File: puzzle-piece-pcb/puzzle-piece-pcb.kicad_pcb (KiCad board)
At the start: 2 copper layers, 27 x 27 mm, 7 parts, among them J1 OLED, J2 Input, J3 PROG_DEBUG, U1 ATtiny1624-SS

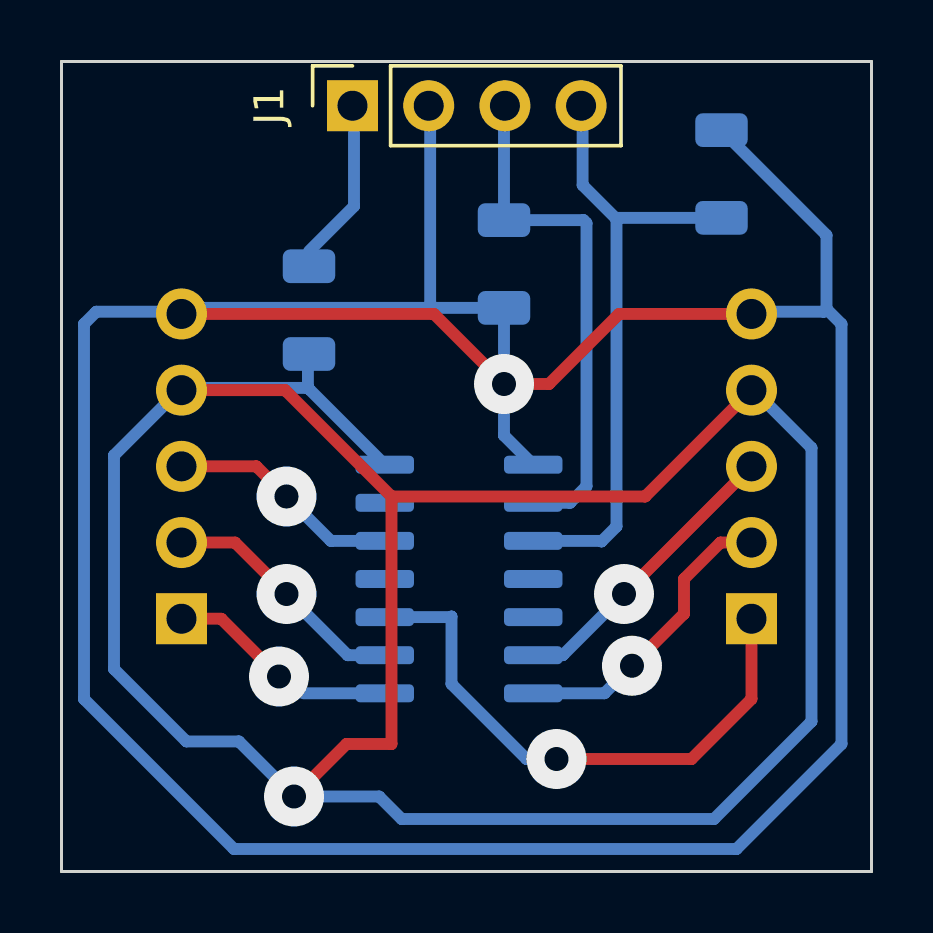
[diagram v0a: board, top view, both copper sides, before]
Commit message: made puzzle piece pcb one sided
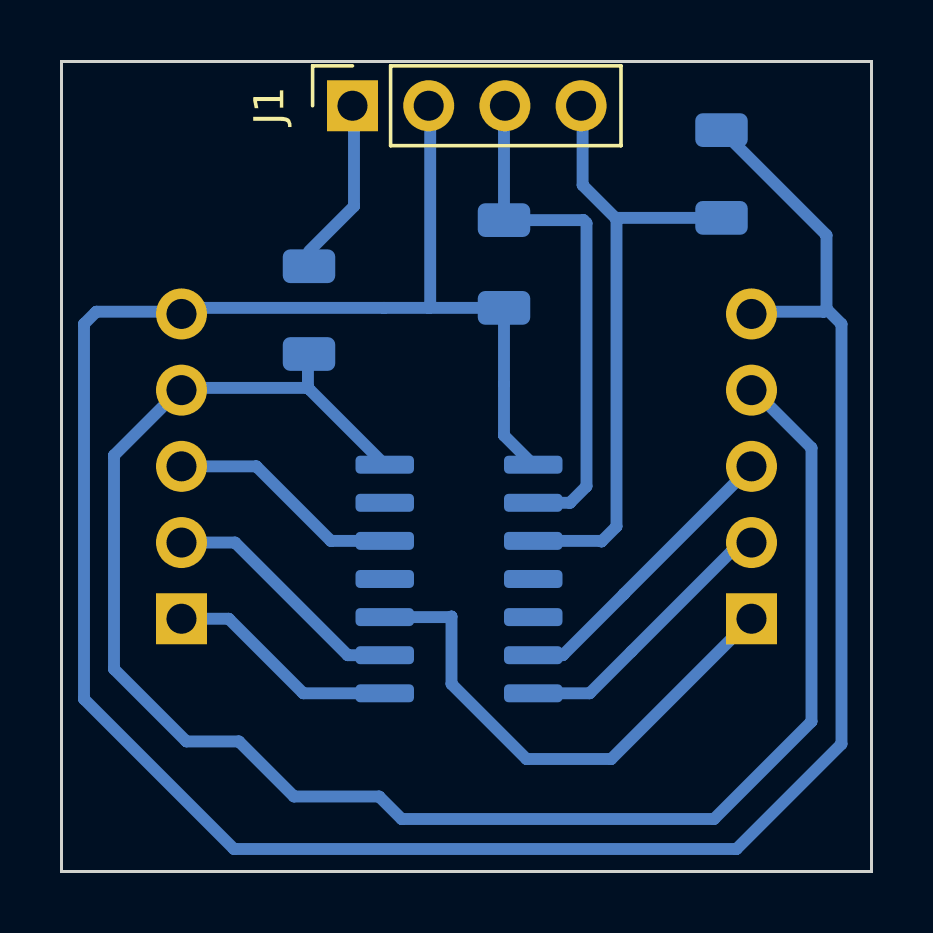
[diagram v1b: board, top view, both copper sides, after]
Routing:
- net OLED_GND : track 97.5 -> 63.3 mm, vias 1 -> 0
- net +3.3V: track 113.4 -> 92.5 mm, vias 1 -> 0
- net UPDI: track 19.0 -> 17.5 mm, vias 1 -> 0
- net H_SDA: track 6.76 -> 7.80 mm, vias 1 -> 0
- net TX: track 10.0 -> 9.36 mm, vias 1 -> 0
- net H_SCL: vias 1 -> 0
- net RX: vias 1 -> 0
- net ANALOG: vias 1 -> 0
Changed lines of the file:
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@@
-	)
-	(segment
-		(start 165 100)
-		(end 166.5 100)
-		(width 0.396748)
-		(layer "F.Cu")
-		(net 3)
-	)
-	(segment
-		(start 154.25 97.665)
-		(end 162.665 97.665)
-		(width 0.396748)
-		(layer "F.Cu")
-		(net 3)
-	)
-	(segment
-		(start 166.5 100)
-		(end 168.835 97.665)
-		(width 0.396748)
-		(layer "F.Cu")
-		(net 3)
-	)
-	(segment
-		(start 168.835 97.665)
-		(end 173.25 97.665)
-		(width 0.396748)
-		(layer "F.Cu")
-		(net 3)
-	)
-	(segment
-		(start 162.665 97.665)
-		(end 165 100)
-		(width 0.396748)
-		(layer "F.Cu")
-		(net 3)
-	)
-	(via
-		(at 165 100)
-		(size 2)
-		(drill 0.8)
-		(layers "F.Cu" "B.Cu")
-		(net 3)
 	)
 	(segment
@@
 	)
 	(segment
-		(start 154.25 102.745)
-		(end 156.745 102.745)
-		(width 0.396748)
-		(layer "F.Cu")
-		(net 4)
-	)
-	(segment
-		(start 156.745 102.745)
-		(end 157.75 103.75)
-		(width 0.396748)
-		(layer "F.Cu")
-		(net 4)
-	)
-	(via
-		(at 157.75 103.75)
-		(size 2)
-		(drill 0.8)
-		(layers "F.Cu" "B.Cu")
-		(net 4)
-	)
-	(segment
 		(start 161.025 105.23)
 		(end 159.23 105.23)
@@
 	(segment
 		(start 159.23 105.23)
-		(end 157.75 103.75)
+		(end 156.745 102.745)
 		(width 0.396748)
 		(layer "B.Cu")
@@
 	)
 	(segment
-		(start 154.25 107.825)
-		(end 155.575 107.825)
-		(width 0.396748)
-		(layer "F.Cu")
-		(net 5)
-	)
-	(segment
-		(start 155.575 107.825)
-		(end 157.5 109.75)
-		(width 0.396748)
-		(layer "F.Cu")
-		(net 5)
-	)
-	(via
-		(at 157.5 109.75)
-		(size 2)
-		(drill 0.8)
-		(layers "F.Cu" "B.Cu")
-		(net 5)
+		(start 156.745 102.745)
+		(end 154.25 102.745)
+		(width 0.396748)
+		(layer "B.Cu")
+		(net 4)
 	)
 	(segment
@@
 	)
 	(segment
-		(start 154.25 105.285)
+		(start 155.825 107.825)
+		(end 154.25 107.825)
+		(width 0.396748)
+		(layer "B.Cu")
+		(net 5)
+	)
+	(segment
+		(start 158.31 110.31)
+		(end 155.825 107.825)
+		(width 0.396748)
+		(layer "B.Cu")
+		(net 5)
+	)
+	(segment
+		(start 159.79 109.04)
 		(end 156.035 105.285)
 		(width 0.396748)
-		(layer "F.Cu")
+		(layer "B.Cu")
 		(net 6)
 	)
 	(segment
+		(start 161.025 109.04)
+		(end 159.79 109.04)
+		(width 0.396748)
+		(layer "B.Cu")
+		(net 6)
+	)
+	(segment
 		(start 156.035 105.285)
-		(end 157.75 107)
-		(width 0.396748)
-		(layer "F.Cu")
+		(end 154.25 105.285)
+		(width 0.396748)
+		(layer "B.Cu")
 		(net 6)
 	)
-	(via
-		(at 157.75 107)
-		(size 2)
-		(drill 0.8)
-		(layers "F.Cu" "B.Cu")
-		(net 6)
-	)
-	(segment
-		(start 159.79 109.04)
-		(end 157.75 107)
-		(width 0.396748)
-		(layer "B.Cu")
-		(net 6)
-	)
-	(segment
-		(start 159.79 109.04)
-		(end 161.025 109.04)
-		(width 0.396748)
-		(layer "B.Cu")
-		(net 6)
-	)
-	(segment
-		(start 171 107.657427)
-		(end 171 106.5)
-		(width 0.396748)
-		(layer "F.Cu")
+	(segment
+		(start 167.855452 110.31)
+		(end 165.975 110.31)
+		(width 0.396748)
+		(layer "B.Cu")
 		(net 7)
 	)
 	(segment
-		(start 171 106.5)
-		(end 172.215 105.285)
-		(width 0.396748)
-		(layer "F.Cu")
+		(start 169.25 108.915452)
+		(end 172.880452 105.285)
+		(width 0.396748)
+		(layer "B.Cu")
 		(net 7)
 	)
 	(segment
-		(start 172.215 105.285)
+		(start 172.880452 105.285)
 		(end 173.25 105.285)
 		(width 0.396748)
-		(layer "F.Cu")
+		(layer "B.Cu")
 		(net 7)
 	)
 	(segment
-		(start 169.265743 109.391684)
-		(end 171 107.657427)
-		(width 0.396748)
-		(layer "F.Cu")
+		(start 169.25 108.915452)
+		(end 167.855452 110.31)
+		(width 0.396748)
+		(layer "B.Cu")
 		(net 7)
 	)
-	(via
-		(at 169.265743 109.391684)
-		(size 2)
-		(drill 0.8)
-		(layers "F.Cu" "B.Cu")
-		(net 7)
-	)
-	(segment
-		(start 169.265743 109.391684)
-		(end 168.347427 110.31)
-		(width 0.396748)
-		(layer "B.Cu")
-		(net 7)
-	)
-	(segment
-		(start 168.347427 110.31)
-		(end 165.975 110.31)
-		(width 0.396748)
-		(layer "B.Cu")
-		(net 7)
+	(segment
+		(start 169 106.995)
+		(end 173.25 102.745)
+		(width 0.396748)
+		(layer "B.Cu")
+		(net 8)
+	)
+	(segment
+		(start 166.96 109.04)
+		(end 169 107)
+		(width 0.396748)
+		(layer "B.Cu")
+		(net 8)
+	)
+	(segment
+		(start 166.25 109)
+		(end 166.21 109.04)
+		(width 0.396748)
+		(layer "B.Cu")
+		(net 8)
 	)
 	(segment
@@
 		(end 169 106.995)
 		(width 0.396748)
-		(layer "F.Cu")
-		(net 8)
-	)
-	(segment
-		(start 169 106.995)
-		(end 173.25 102.745)
-		(width 0.396748)
-		(layer "F.Cu")
-		(net 8)
-	)
-	(via
-		(at 169 107)
-		(size 2)
-		(drill 0.8)
-		(layers "F.Cu" "B.Cu")
-		(net 8)
-	)
-	(segment
-		(start 166.96 109.04)
-		(end 169 107)
-		(width 0.396748)
-		(layer "B.Cu")
-		(net 8)
-	)
-	(segment
-		(start 166.25 109)
-		(end 166.21 109.04)
-		(width 0.396748)
 		(layer "B.Cu")
 		(net 8)
@@
 	)
 	(segment
-		(start 173.25 110.5)
-		(end 171.25 112.5)
-		(width 0.396748)
-		(layer "F.Cu")
-		(net 9)
-	)
-	(segment
-		(start 173.25 107.825)
-		(end 173.25 110.5)
-		(width 0.396748)
-		(layer "F.Cu")
-		(net 9)
-	)
-	(segment
-		(start 171.25 112.5)
-		(end 166.75 112.5)
-		(width 0.396748)
-		(layer "F.Cu")
-		(net 9)
-	)
-	(via
-		(at 166.75 112.5)
-		(size 2)
-		(drill 0.8)
-		(layers "F.Cu" "B.Cu")
+		(start 165.75 112.5)
+		(end 168.575 112.5)
+		(width 0.396748)
+		(layer "B.Cu")
+		(net 9)
+	)
+	(segment
+		(start 168.575 112.5)
+		(end 173.25 107.825)
+		(width 0.396748)
+		(layer "B.Cu")
 		(net 9)
 	)
@@
 	)
 	(segment
+		(start 163.25 110)
+		(end 165.75 112.5)
+		(width 0.396748)
+		(layer "B.Cu")
+		(net 9)
+	)
+	(segment
 		(start 161.025 107.77)
 		(end 163.23 107.77)
@@
 	)
 	(segment
-		(start 165.75 112.5)
-		(end 166.75 112.5)
-		(width 0.396748)
-		(layer "B.Cu")
-		(net 9)
-	)
-	(segment
 		(start 163.25 107.75)
 		(end 163.25 110)
@@
 	)
 	(segment
-		(start 163.25 110)
-		(end 165.75 112.5)
-		(width 0.396748)
-		(layer "B.Cu")
-		(net 9)
-	)
-	(segment
-		(start 161.25 112)
-		(end 159.75 112)
-		(width 0.396748)
-		(layer "F.Cu")
-		(net 14)
-	)
-	(segment
-		(start 157.705 100.205)
-		(end 161.25 103.75)
-		(width 0.396748)
-		(layer "F.Cu")
-		(net 14)
-	)
-	(segment
-		(start 161.25 103.75)
-		(end 169.705 103.75)
-		(width 0.396748)
-		(layer "F.Cu")
-		(net 14)
-	)
-	(segment
-		(start 169.705 103.75)
-		(end 173.25 100.205)
-		(width 0.396748)
-		(layer "F.Cu")
-		(net 14)
-	)
-	(segment
-		(start 154.25 100.205)
-		(end 157.705 100.205)
-		(width 0.396748)
-		(layer "F.Cu")
-		(net 14)
-	)
-	(segment
-		(start 159.75 112)
-		(end 158 113.75)
-		(width 0.396748)
-		(layer "F.Cu")
-		(net 14)
-	)
-	(segment
-		(start 161.25 103.75)
-		(end 161.25 112)
-		(width 0.396748)
-		(layer "F.Cu")
-		(net 14)
-	)
-	(via
-		(at 158 113.75)
-		(size 2)
-		(drill 0.8)
-		(layers "F.Cu" "B.Cu")
-		(net 14)
-	)
-	(segment

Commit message: made battery controller singled sided and removed lipo
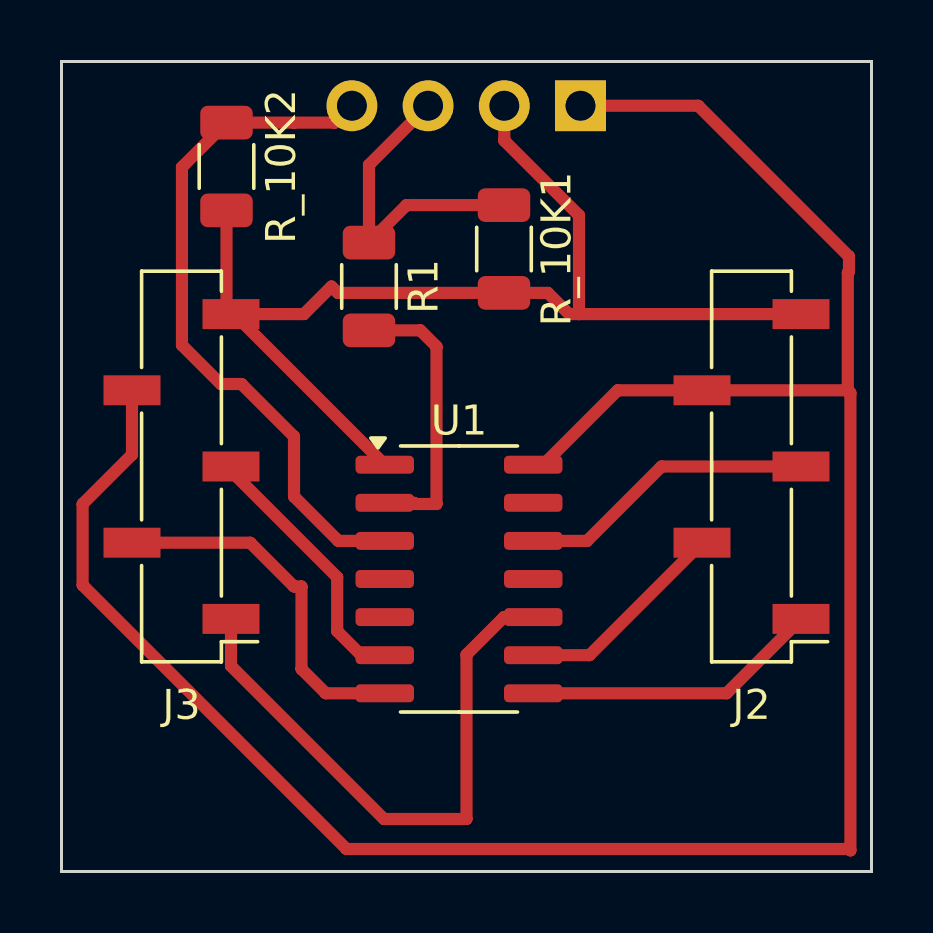
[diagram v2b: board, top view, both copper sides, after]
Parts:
- J1: moved to B.Cu
- J2, J3: footprint Connector_PinHeader_2.54mm:PinHeader_1x05_P2.54mm_Vertical -> Connector_PinSocket_2.54mm:PinSocket_1x05_P2.54mm_Vertical_SMD_Pin1Left; moved to F.Cu
- R1, R_10K1, R_10K2, U1: moved to F.Cu
- moved J2 19.7 mm to (173.2, 102.8), turned to 180 degrees
- moved J3 19.7 mm to (154.2, 102.8), turned to 180 degrees
- moved R_10K2 16.5 mm to (155.8, 92.8), turned to -90 degrees
- moved J1 7.60 mm to (167.6, 90.7)
- moved R1 2.15 mm to (160.5, 96.8)
- moved R_10K1 0.50 mm to (165.0, 95.5)
- turned U1 to 0 degrees
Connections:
- R1 pad 1: OLED_GND  -> S_SCL
- R1 pad 2: OLED_GND  -> Net-(U1-PA4)
- U1 pad 2: S_SCL -> Net-(U1-PA4)
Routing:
- net +3.3V: track 92.5 -> 38.7 mm
- net OLED_GND : track 63.3 -> 78.8 mm
- net Net-(U1-PA4): track 0.00 -> 9.46 mm
- net S_SCL: track 17.4 -> 10.4 mm
- net TX: track 9.36 -> 12.1 mm
- net UPDI: track 17.5 -> 19.8 mm
- net H_SDA: track 7.80 -> 9.95 mm
- net ANALOG: track 7.80 -> 9.95 mm
- net S_SDA: track 21.0 -> 23.1 mm
- net H_SCL: track 8.33 -> 7.18 mm
- net RX: track 9.94 -> 8.87 mm

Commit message: current puzzle with attiny and pogo pins
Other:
- outline, holes or cut-outs redrawn
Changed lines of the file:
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@@
 		(tags "Surface mounted socket strip SMD 1x05 2.54mm single row style1 pin1 left")
 		(property "Reference" "J2"
-			(at 0 -7.95 360)
+			(at 0 -7.95 0)
 			(layer "F.SilkS")
 			(effects
@@
 		)
 		(property "Value" "Input"
-			(at 0 7.95 360)
+			(at 0 7.95 0)
 			(layer "F.Fab")
 			(effects
@@
 		)
 	)
+	(gr_circle
+		(center 152.75 113.75)
+		(end 152.75 114.75)
+		(stroke
+			(width 0.05)
+			(type default)
+		)
+		(fill none)
+		(layer "Edge.Cuts")
+	)
+	(gr_line
+		(start 151.158031 116.225057)
+		(end 151.16 116.25)
+		(stroke
+			(width 0.05)
+			(type default)
+		)
+		(layer "Edge.Cuts")
+	)
+	(gr_circle
+		(center 174.75 91.75)
+		(end 175.75 91.75)
+		(stroke
+			(width 0.05)
+			(type default)
+		)
+		(fill none)
+		(layer "Edge.Cuts")
+	)
 	(gr_rect
 		(start 150.25 89.25)
 		(end 177.25 116.25)
 		(stroke
-			(width 0.1)
+			(width 0.05)
 			(type default)
 		)
@@
 		)
 		(height -0.25)
-		(gr_text "1062.9921 mils"
+		(gr_text "27.0000 mm"
 			(at 149.15 102.75 90)
 			(layer "F.SilkS")
@@
 		)
 		(height 0)
-		(gr_text "1062.9921 mils"
+		(gr_text "27.0000 mm"
 			(at 163.75 88.15 0)
 			(layer "F.SilkS")
@@
 	)
 	(segment
-		(start 176.46 96.29)
-		(end 176.46 100.21)
-		(width 0.4064)
-		(layer "F.Cu")
-		(net 14)
-	)
-	(segment
 		(start 176.46 100.21)
 		(end 176.5468 100.2968)
@@
 	)
 	(segment
-		(start 171.475 90.725)
-		(end 176.5 95.75)
+		(start 172.4 96.03)
+		(end 176.46 96.03)
 		(width 0.4064)
 		(layer "F.Cu")
@@
 	)
 	(segment
-		(start 176.5 95.75)
-		(end 176.5 96.25)
+		(start 167.55 90.725)
+		(end 167.55 91.18)
 		(width 0.4064)
 		(layer "F.Cu")
@@
 	)
 	(segment
-		(start 176.5 96.25)
-		(end 176.46 96.29)
-		(width 0.4064)
-		(layer "F.Cu")
-		(net 14)
-	)
-	(segment
 		(start 165.975 102.69)
 		(end 166.31 102.69)
@@
 	)
 	(segment
+		(start 176.46 96.03)
+		(end 176.46 100.21)
+		(width 0.4064)
+		(layer "F.Cu")
+		(net 14)
+	)
+	(segment
+		(start 167.55 91.18)
+		(end 172.4 96.03)
+		(width 0.4064)
+		(layer "F.Cu")
+		(net 14)
+	)
+	(segment
 		(start 150.9532 106.7032)
 		(end 159.75 115.5)
@@
 		(width 0.4064)
 		(layer "F.Cu")
-		(net 14)
-	)
-	(segment
-		(start 167.55 90.725)
-		(end 171.475 90.725)
-		(width 0.4064)
-		(layer "F.Cu")
